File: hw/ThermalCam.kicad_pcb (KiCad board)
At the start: 4 copper layers, 44.9 x 47.2 mm, 131 parts, among them J1 Conn_02x20_Counter_Clockwise, J2 Conn_01x04, J3 Conn_01x06, J4 USB_C_Receptacle, Q1 BSS138PW,115, U1 GW1NR-9_QN882, U2 MUN3CAD01-SC, U3 MUN3CAD01-SC, U4 MUN3CAD01-SC, U5 AP3012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

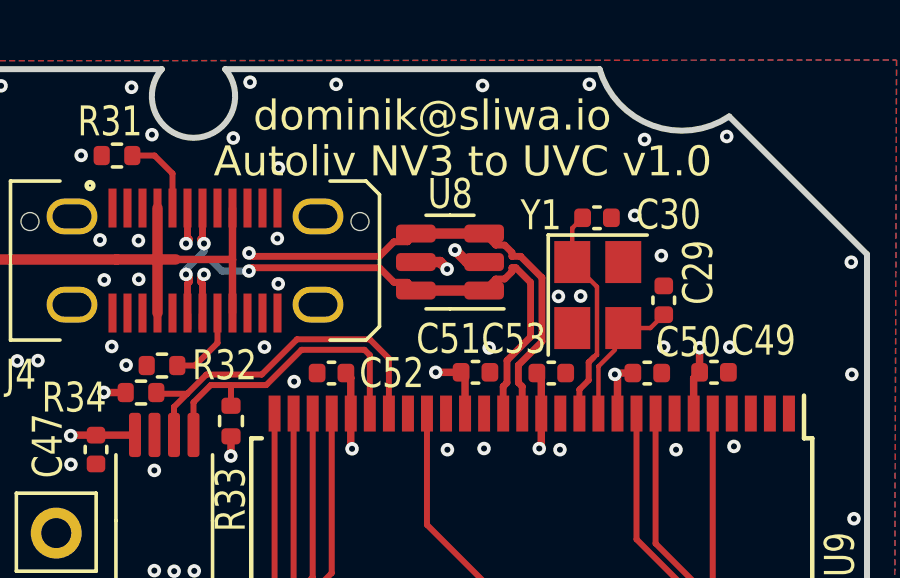
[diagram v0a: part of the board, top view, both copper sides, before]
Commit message: working UVC demo
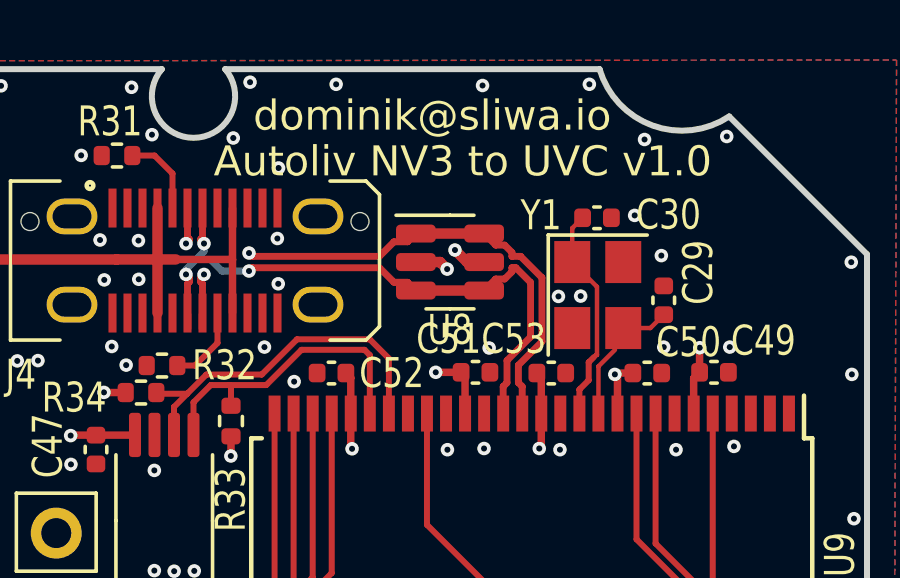
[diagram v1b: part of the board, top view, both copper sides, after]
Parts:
- R23: value 31k6 -> 22k1
- R4: value 1k -> 5k1
- turned U8 to 0 degrees
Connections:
- U8 pad 1: /USB/USB_D- -> /USB/USB_D+
- U8 pad 2: +5V -> GND
- U8 pad 3: /USB/USB_D+ -> /USB/USB_D-
- U8 pad 4: /USB/USB_D+ -> /USB/USB_D-
- U8 pad 5: GND -> +5V
- U8 pad 6: /USB/USB_D- -> /USB/USB_D+
